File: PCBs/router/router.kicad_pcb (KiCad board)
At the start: 2 copper layers, 95.3 x 110 mm, 37 parts, among them J1 Conn_01x06_Male, J10 Conn_01x06_Male, J11 Conn_01x06_Male, J12 Conn_01x06_Male, J13 Conn_01x06_Male, J14 Conn_01x06_Male, J15 Conn_01x06_Male, J2 Conn_01x06_Male, J3 Conn_01x06_Male, J4 Conn_01x06_Male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

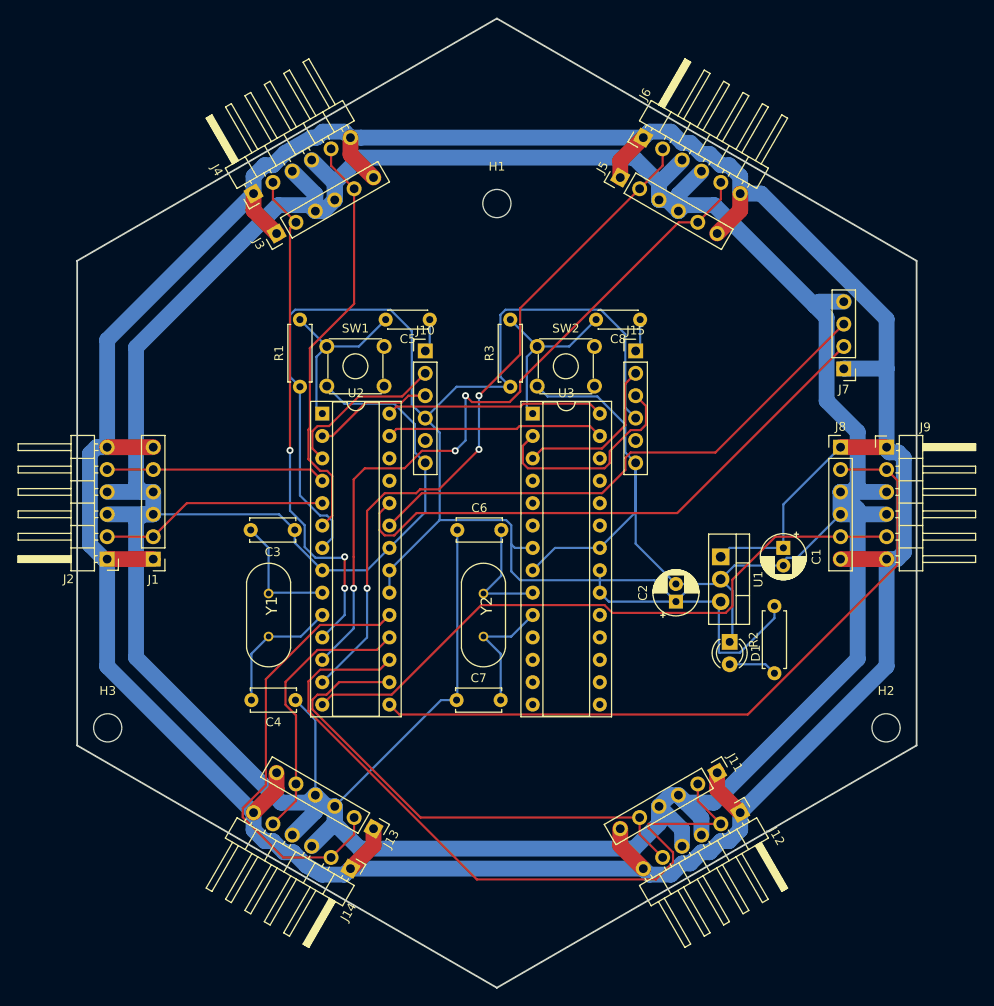
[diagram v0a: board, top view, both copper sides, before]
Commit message: move actor port and power regulator
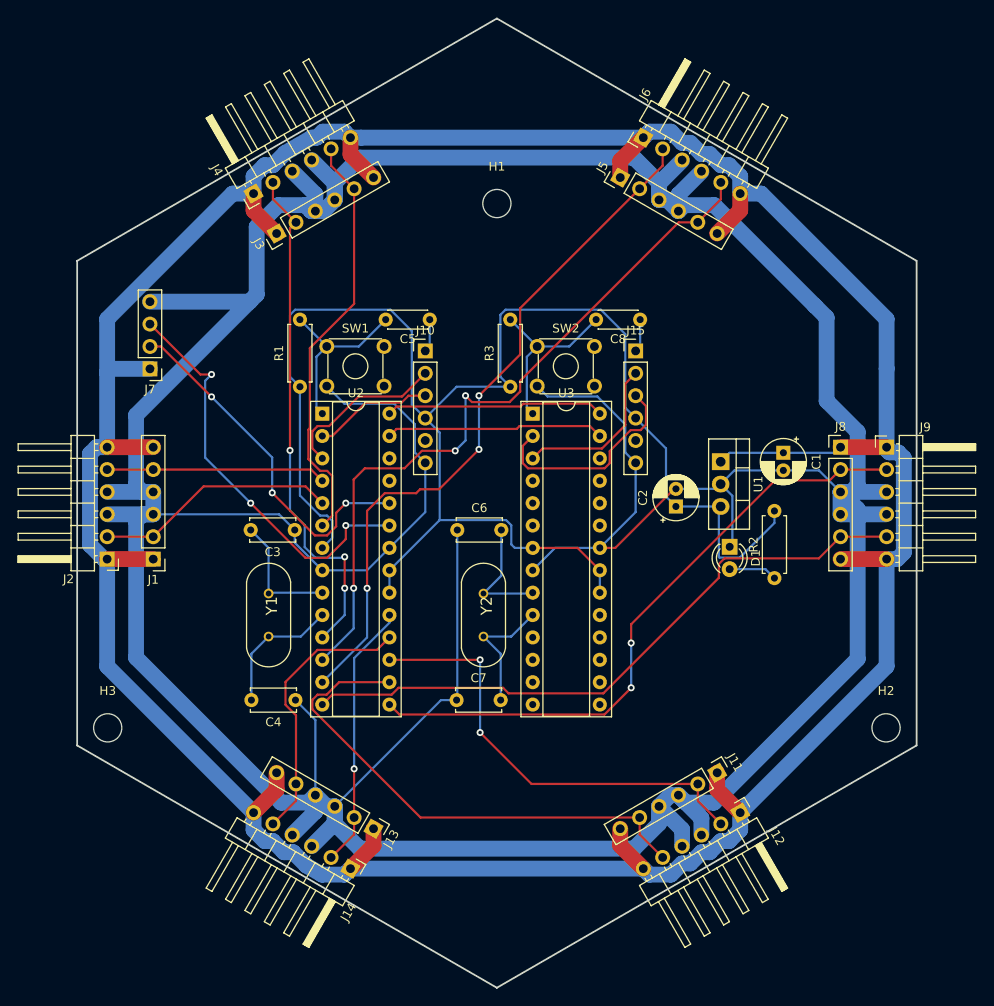
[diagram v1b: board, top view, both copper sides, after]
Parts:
- moved J7 78.7 mm to (113.0, 86.4)
- moved C1 10.8 mm to (184.9, 95.9)
- moved C2 10.8 mm to (172.7, 102.0)
- moved D1 10.8 mm to (178.8, 106.6)
- moved R2 10.8 mm to (183.9, 110.1)
- moved U1 10.8 mm to (177.8, 96.9)
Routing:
- net Net-(J11-Pad2): track 83.0 -> 51.3 mm, vias 0 -> 2
- net Net-(J7-Pad2): track 65.4 -> 41.0 mm, vias 0 -> 3
- net Net-(J13-Pad2): track 51.3 -> 30.3 mm, vias 0 -> 1
- net Net-(J7-Pad3): track 61.8 -> 47.1 mm, vias 0 -> 3
- net Net-(C2-Pad1): track 192.8 -> 179.6 mm
- net Net-(J8-Pad2): track 81.7 -> 72.6 mm, vias 0 -> 2
- net +9V: track 394.6 -> 388.8 mm
- net GND: track 545.4 -> 547.9 mm
- net Net-(J1-Pad2): track 26.0 -> 27.6 mm
- net Net-(J8-Pad5): track 74.4 -> 73.4 mm

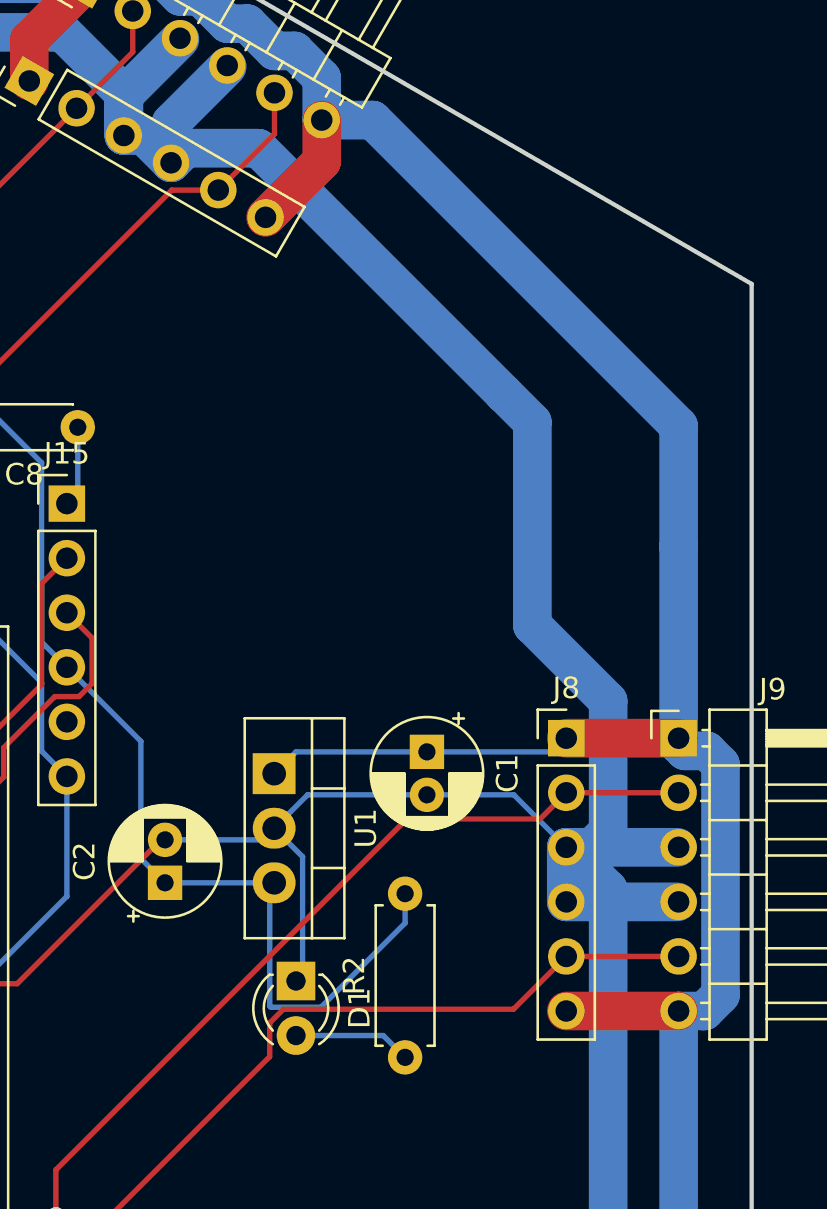
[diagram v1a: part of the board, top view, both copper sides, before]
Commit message: cleaning some traces
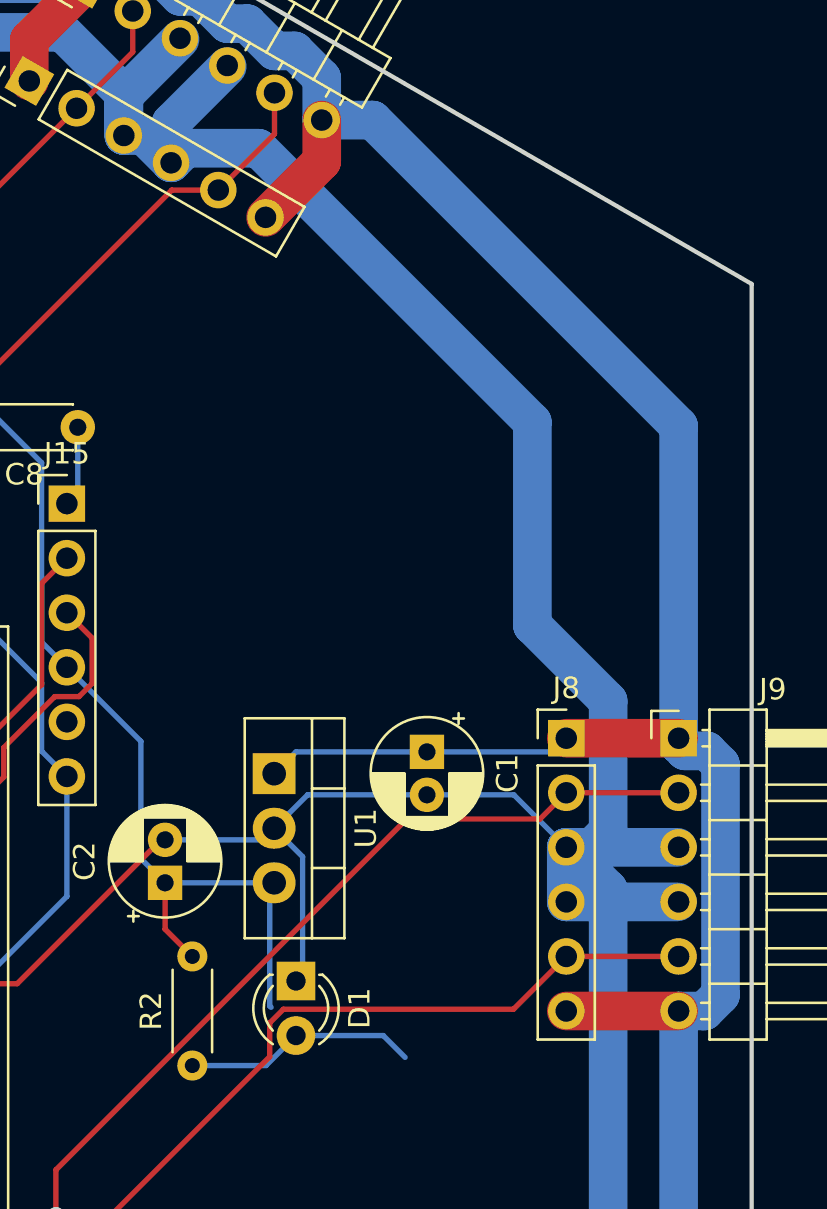
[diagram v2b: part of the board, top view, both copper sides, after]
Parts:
- R2: footprint Resistor_THT:R_Axial_DIN0207_L6.3mm_D2.5mm_P7.62mm_Horizontal -> Resistor_THT:R_Axial_DIN0204_L3.6mm_D1.6mm_P5.08mm_Horizontal
- moved R2 9.91 mm to (174.0, 110.5)
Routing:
- net Net-(D1-Pad2): track 5.50 -> 10.9 mm
- net Net-(C2-Pad1): track 179.6 -> 174.3 mm
